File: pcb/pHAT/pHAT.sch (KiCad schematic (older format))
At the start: 45 parts, among them M1 mount1, M2 mount1, M3 mount1, M4 mount1, P2 USB_A, P3 USB_B, P4 CONN_01X30, Q1 XTL, U1 FE1.1S, U2 ATTINY102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

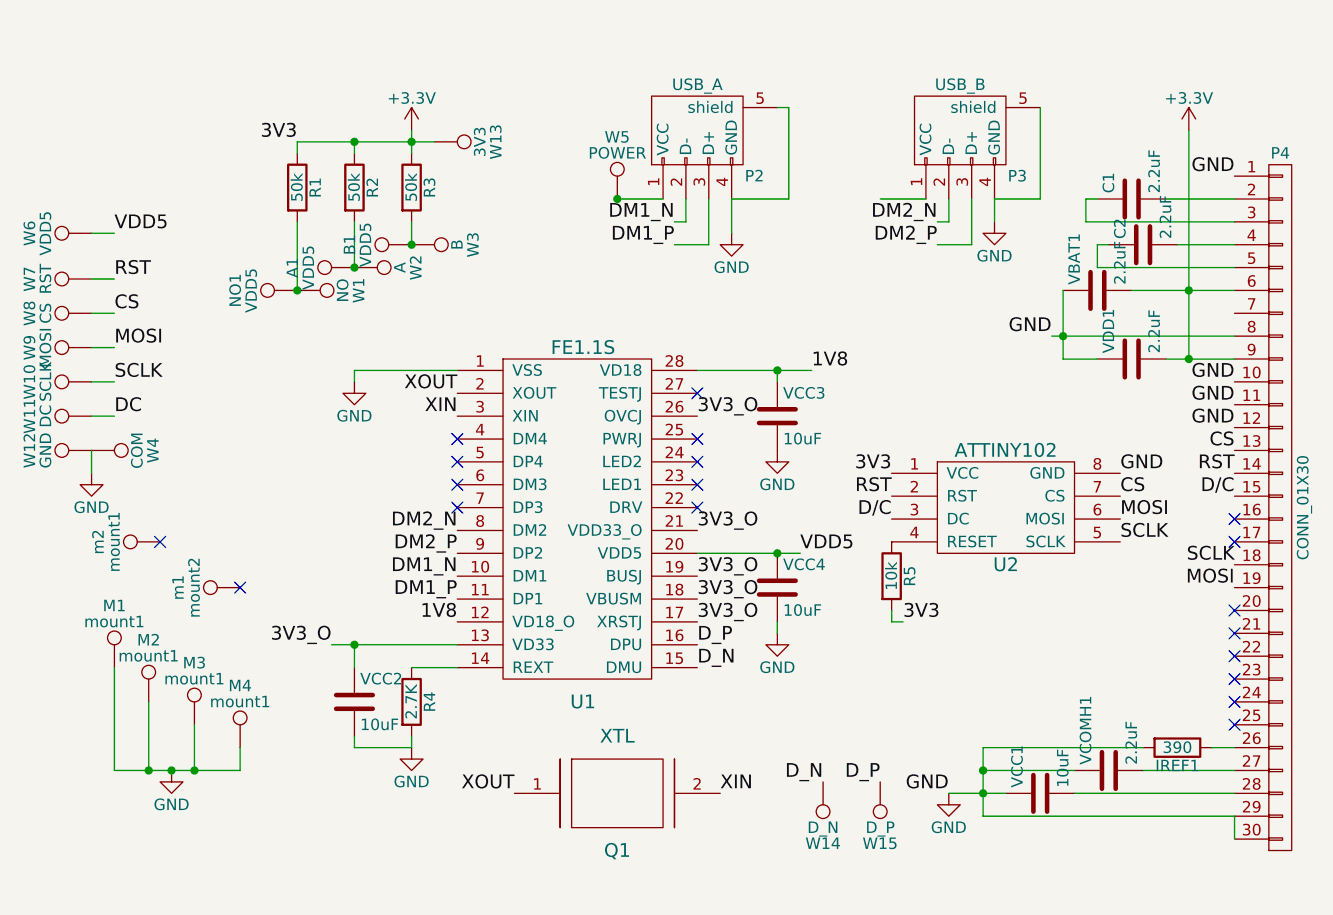
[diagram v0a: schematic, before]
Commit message: PCB layout with buttons
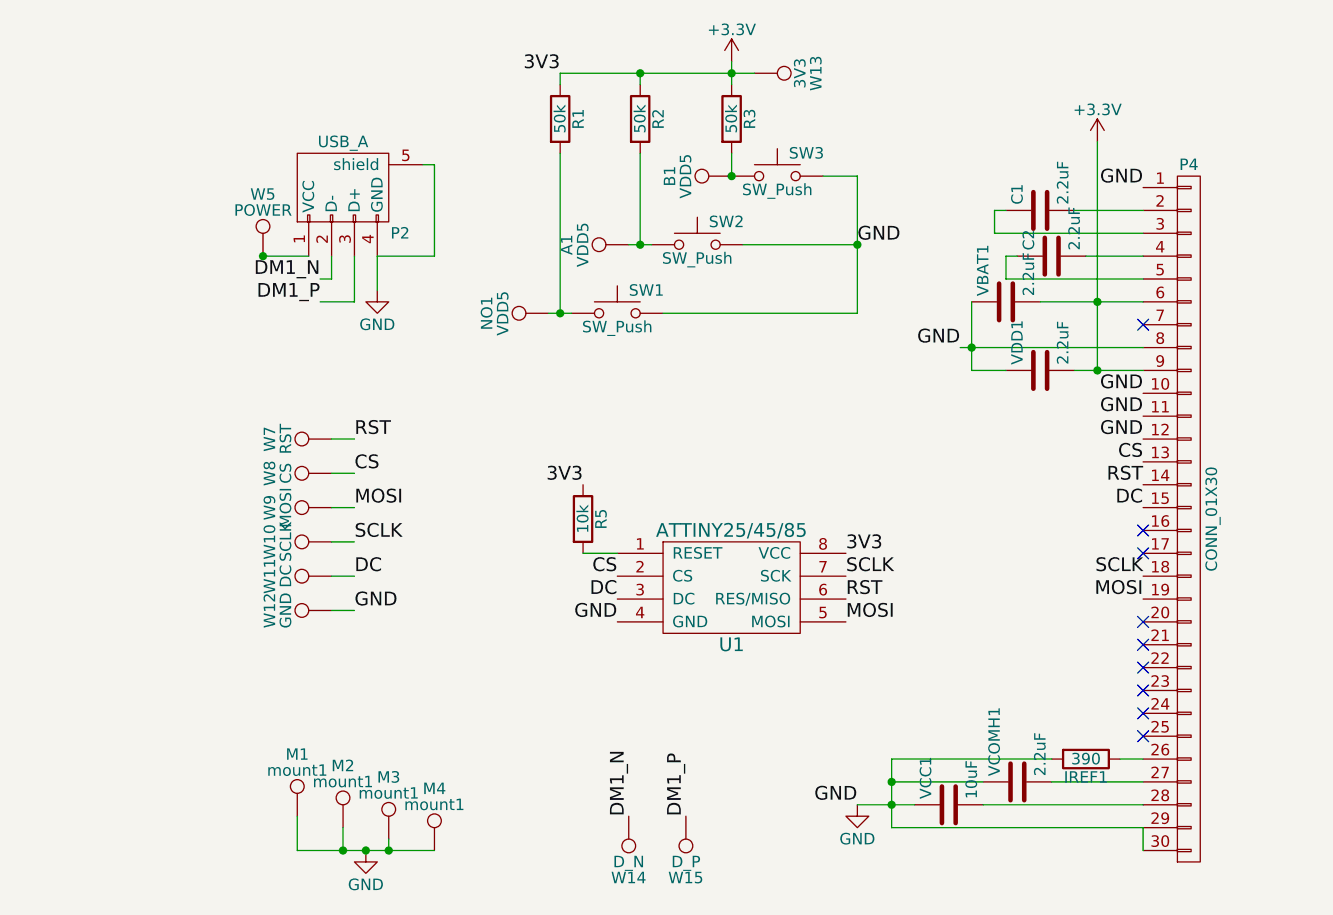
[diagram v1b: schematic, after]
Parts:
- removed P3: USB_B, pISO:usb_micro, symbol USB_B-RESCUE-pHAT
- removed Q1: XTL, Crystals:Crystal_SMD_HC49-SD, symbol XTL
- removed R4: 2.7K, Resistors_SMD:R_0805, symbol R
- removed U1: FE1.1S, Housings_SSOP:SSOP-28_3.9x9.9mm_Pitch0.635mm, symbol FE1.1S-RESCUE-pHAT
- removed U2: ATTINY102, Housings_SOIC:SOIC-8_3.9x4.9mm_Pitch1.27mm, symbol ATTINY102
- removed VCC2, VCC3, VCC4: 10uF, Capacitors_SMD:C_0805, symbol C
- removed W1: NO, pISO:swpins, symbol TEST_1P
- removed W2: A, pISO:swpins, symbol TEST_1P
- removed W3: B, pISO:swpins, symbol TEST_1P
- removed W4: COM, pISO:swpins, symbol TEST_1P
- removed W6: VDD5, pISO:SLP, symbol TEST_1P
- removed m1: mount2, pISO:swpins, symbol TEST_1P
- removed m2: mount1, pISO:swpins, symbol TEST_1P
- added SW1, SW2, SW3: SW_Push, pISO:spst, symbol SW_Push
- added U1: ATTINY25/45/85, Housings_SOIC:SOIJ-8_5.3x5.3mm_Pitch1.27mm, symbol ATTINY25/45/85
- A1, B1, NO1, W10, W11, W12, W13, W14, W15, W7, W8, W9: Price .30 -> .28
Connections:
- net D/C is gone; now on net DC: P4.15 (P15)
- net D_N is gone; now on net DM1_N: W14.1
- net D_P is gone; now on net DM1_P: W15.1
- net +3V3: now also R5.1, U1.8 (VCC); no longer R5.2
- net CS: now also U1.2 (CS)
- net DC: now also U1.3 (DC)
- net GND: now also SW1.2, SW2.2, SW3.2, U1.4 (GND)
- net MOSI: now also U1.5 (MOSI)
- net RST: now also U1.6 (RES/MISO)
- net SCLK: now also U1.7 (SCK)
- net at A1.1, R2.2: now also SW2.1
- net at B1.1, R3.2: now also SW3.1
- net at NO1.1, R1.2: now also SW1.1
- new net: R5.2, U1.1 (RESET)
- no-connect marks 19 -> 9
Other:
- moved on the sheet: A1, B1, C1, C2, IREF1, M1, M2, M3, M4, NO1, P2, P4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

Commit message: update for USBA board
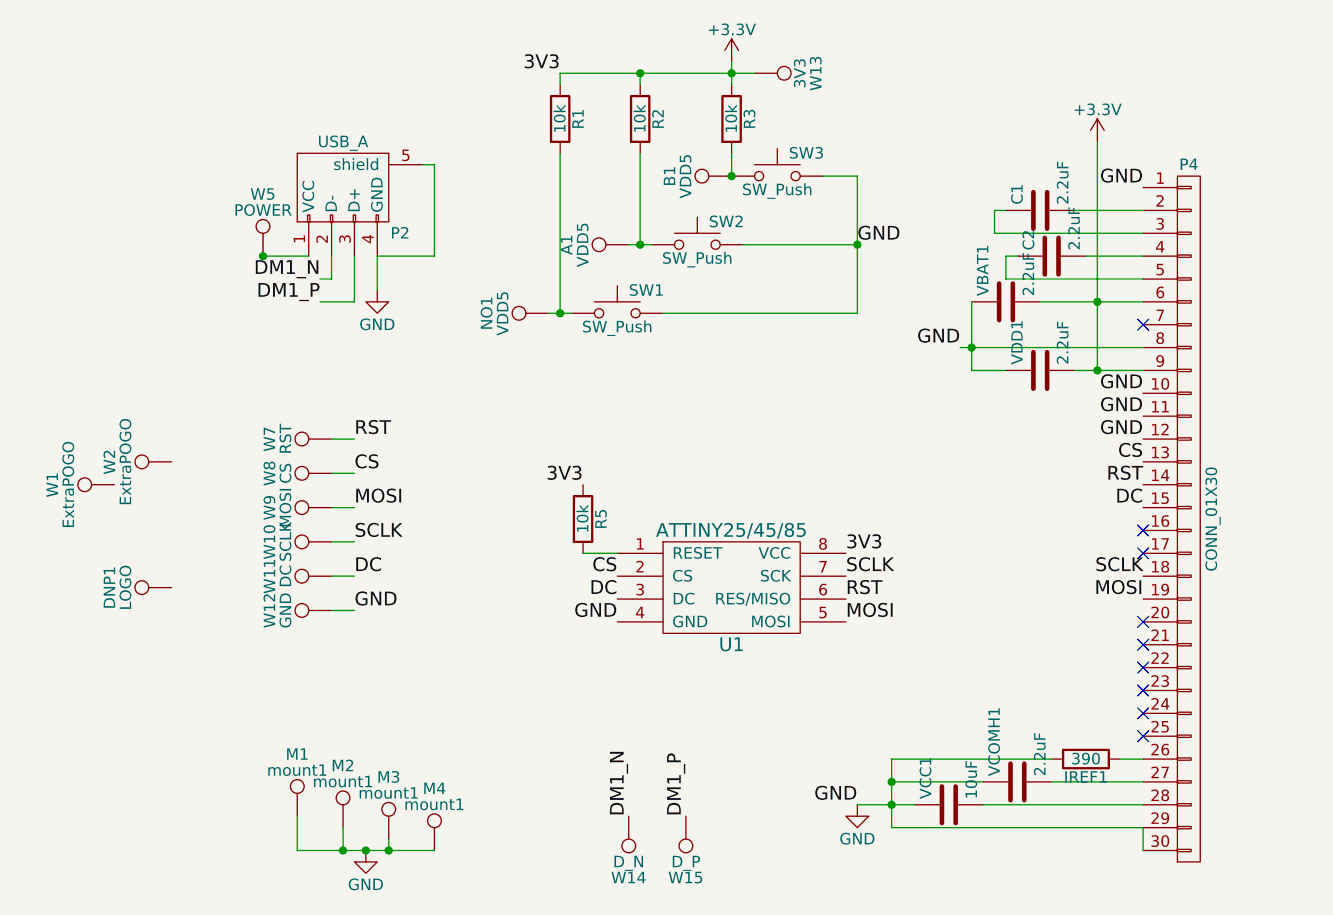
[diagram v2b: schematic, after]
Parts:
- added DNP1: LOGO, pISO:LOGO, symbol TEST_1P
- added W1, W2: ExtraPOGO, pISO:SLP, symbol TEST_1P
- R1, R2, R3: value 50k -> 10k
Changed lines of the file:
@@
 EESchema Schematic File Version 2
 LIBS:pHAT-rescue
-LIBS:pISO
 LIBS:analog_switches
 LIBS:switches
+LIBS:pISO
 LIBS:pHAT-cache
 EELAYER 25 0
@@
 $EndDescr
 $Comp
-L GND #PWR01
+L GND #PWR2
 U 1 1 59A62435
 P 2950 3350
-F 0 "#PWR01" H 2950 3100 50  0001 C CNN
+F 0 "#PWR2" H 2950 3100 50  0001 C CNN
 F 1 "GND" H 2950 3200 50  0000 C CNN
 F 2 "" H 2950 3350 50  0000 C CNN
@@
 $EndComp
 $Comp
-L +3.3V #PWR02
+L +3.3V #PWR5
 U 1 1 59AC5DDC
 P 6100 2700
-F 0 "#PWR02" H 6100 2550 50  0001 C CNN
+F 0 "#PWR5" H 6100 2550 50  0001 C CNN
 F 1 "+3.3V" H 6100 2840 50  0000 C CNN
 F 2 "" H 6100 2700 50  0000 C CNN
@@
 Text Label 6300 2900 2    60   ~ 0
 GND
-$Comp
-L R R3
-U 1 1 59F0071D
-P 4500 2600
-F 0 "R3" V 4580 2600 50  0000 C CNN
-F 1 "50k" V 4500 2600 50  0000 C CNN
-F 2 "Resistors_SMD:R_0805" V 4430 2600 50  0001 C CNN
-F 3 "https://www.digikey.com/product-detail/en/stackpole-electronics-inc/RMCF0805JT51K0/RMCF0805JT51K0CT-ND/1942589" H 4500 2600 50  0001 C CNN
-F 4 ".006" V 4500 2600 60  0001 C CNN "Price"
-	1    4500 2600
-	1    0    0    -1
-$EndComp
-$Comp
-L R R2
-U 1 1 59F007D4
-P 4100 2600
-F 0 "R2" V 4180 2600 50  0000 C CNN
-F 1 "50k" V 4100 2600 50  0000 C CNN
-F 2 "Resistors_SMD:R_0805" V 4030 2600 50  0001 C CNN
-F 3 "https://www.digikey.com/product-detail/en/stackpole-electronics-inc/RMCF0805JT51K0/RMCF0805JT51K0CT-ND/1942589" H 4100 2600 50  0001 C CNN
-F 4 ".006" V 4100 2600 60  0001 C CNN "Price"
-	1    4100 2600
-	1    0    0    -1
-$EndComp
-$Comp
-L R R1
-U 1 1 59F0084D
-P 3750 2600
-F 0 "R1" V 3830 2600 50  0000 C CNN
-F 1 "50k" V 3750 2600 50  0000 C CNN
-F 2 "Resistors_SMD:R_0805" V 3680 2600 50  0001 C CNN
-F 3 "https://www.digikey.com/product-detail/en/stackpole-electronics-inc/RMCF0805JT51K0/RMCF0805JT51K0CT-ND/1942589" H 3750 2600 50  0001 C CNN
-F 4 ".006" V 3750 2600 60  0001 C CNN "Price"
-	1    3750 2600
-	1    0    0    -1
-$EndComp
 Wire Wire Line
 	2850 4150 2750 4150
@@
 $EndComp
 $Comp
-L GND #PWR03
+L GND #PWR1
 U 1 1 5A09ABEB
 P 2900 5800
-F 0 "#PWR03" H 2900 5550 50  0001 C CNN
+F 0 "#PWR1" H 2900 5550 50  0001 C CNN
 F 1 "GND" H 2900 5650 50  0000 C CNN
 F 2 "" H 2900 5800 50  0000 C CNN
@@
 Connection ~ 2450 3200
 $Comp
-L +3.3V #PWR04
+L +3.3V #PWR3
 U 1 1 5A11071F
 P 4500 2350
-F 0 "#PWR04" H 4500 2200 50  0001 C CNN
+F 0 "#PWR3" H 4500 2200 50  0001 C CNN
 F 1 "+3.3V" H 4500 2490 50  0000 C CNN
 F 2 "" H 4500 2350 50  0000 C CNN
@@
 	2750 4450 2850 4450
 $Comp
-L GND #PWR05
+L GND #PWR4
 U 1 1 5A117A99
 P 5050 5600
-F 0 "#PWR05" H 5050 5350 50  0001 C CNN
+F 0 "#PWR4" H 5050 5350 50  0001 C CNN
 F 1 "GND" H 5050 5450 50  0000 C CNN
 F 2 "" H 5050 5600 50  0000 C CNN
@@
 	1    0    0    -1
 $EndComp
+$Comp
+L R R1
+U 1 1 5AB435AF
+P 3750 2600
+F 0 "R1" V 3830 2600 50  0000 C CNN
+F 1 "10k" V 3750 2600 50  0000 C CNN
+F 2 "Resistors_SMD:R_0805" V 3680 2600 50  0001 C CNN
+F 3 "https://www.digikey.com/product-detail/en/stackpole-electronics-inc/RMCF0805JT10K0/RMCF0805JT10K0CT-ND/1942577" H 3750 2600 50  0001 C CNN
+F 4 ".006" V 3750 2600 60  0001 C CNN "Price"
+	1    3750 2600
+	1    0    0    -1
+$EndComp
+$Comp
+L R R2
+U 1 1 5AB4375B
+P 4100 2600
+F 0 "R2" V 4180 2600 50  0000 C CNN
+F 1 "10k" V 4100 2600 50  0000 C CNN
+F 2 "Resistors_SMD:R_0805" V 4030 2600 50  0001 C CNN
+F 3 "https://www.digikey.com/product-detail/en/stackpole-electronics-inc/RMCF0805JT10K0/RMCF0805JT10K0CT-ND/1942577" H 4100 2600 50  0001 C CNN
+F 4 ".006" V 4100 2600 60  0001 C CNN "Price"
+	1    4100 2600
+	1    0    0    -1
+$EndComp
+$Comp
+L R R3
+U 1 1 5AB437FD
+P 4500 2600
+F 0 "R3" V 4580 2600 50  0000 C CNN
+F 1 "10k" V 4500 2600 50  0000 C CNN
+F 2 "Resistors_SMD:R_0805" V 4430 2600 50  0001 C CNN
+F 3 "https://www.digikey.com/product-detail/en/stackpole-electronics-inc/RMCF0805JT10K0/RMCF0805JT10K0CT-ND/1942577" H 4500 2600 50  0001 C CNN
+F 4 ".006" V 4500 2600 60  0001 C CNN "Price"
+	1    4500 2600
+	1    0    0    -1
+$EndComp
+$Comp
+L TEST_1P W2
+U 1 1 5AB441ED
+P 2050 4100
+F 0 "W2" H 2050 4370 50  0000 C CNN
+F 1 "ExtraPOGO" H 2050 4300 50  0000 C CNN
+F 2 "pISO:SLP" H 2250 4100 50  0001 C CNN
+F 3 "https://www.digikey.com/product-detail/en/mill-max-manufacturing-corp/0906-0-15-20-76-14-11-0/ED8180-ND/1147048" H 2250 4100 50  0001 C CNN
+F 4 ".28" H 2050 4100 60  0001 C CNN "Price"
+	1    2050 4100
+	0    -1   -1   0
+$EndComp
+$Comp
+L TEST_1P DNP1
+U 1 1 5AB442FA
+P 2050 4650
+F 0 "DNP1" H 2050 4920 50  0000 C CNN
+F 1 "LOGO" H 2050 4850 50  0000 C CNN
+F 2 "pISO:LOGO" H 2250 4650 50  0001 C CNN
+F 3 "" H 2250 4650 50  0001 C CNN
+	1    2050 4650
+	0    -1   -1   0
+$EndComp
+$Comp
+L TEST_1P W1
+U 1 1 5AB445A1
+P 1800 4200
+F 0 "W1" H 1800 4470 50  0000 C CNN
+F 1 "ExtraPOGO" H 1800 4400 50  0000 C CNN
+F 2 "pISO:SLP" H 2000 4200 50  0001 C CNN
+F 3 "https://www.digikey.com/product-detail/en/mill-max-manufacturing-corp/0906-0-15-20-76-14-11-0/ED8180-ND/1147048" H 2000 4200 50  0001 C CNN
+F 4 ".28" H 1800 4200 60  0001 C CNN "Price"
+	1    1800 4200
+	0    -1   -1   0
+$EndComp
 $EndSCHEMATC
